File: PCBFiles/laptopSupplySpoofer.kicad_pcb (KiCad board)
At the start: 2 copper layers, 26 x 16.5 mm, 4 parts, among them J1 Screw_Terminal_01x02, J2 Screw_Terminal_01x03, U1 DS2431

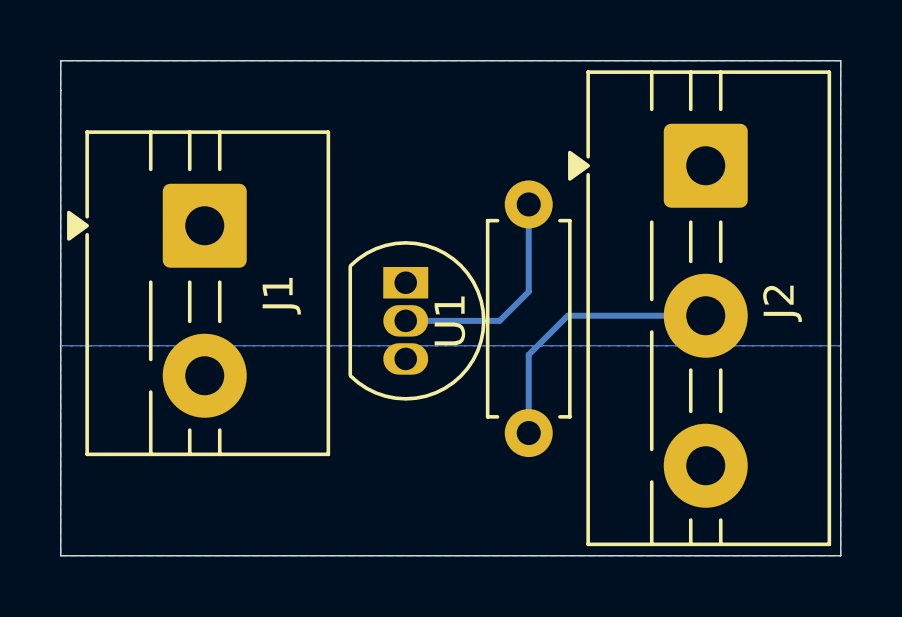
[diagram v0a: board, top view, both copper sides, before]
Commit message: removed delay_us source files and integrated it into ds2431.c for a more clean build also updated PCB files
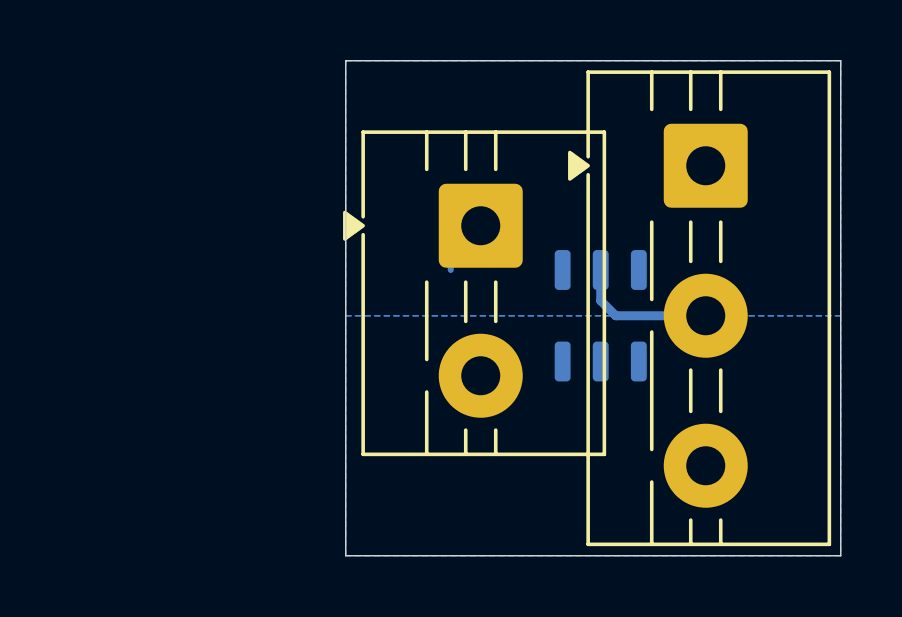
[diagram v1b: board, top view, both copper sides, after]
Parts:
- removed R1: 130, Resistor_THT:R_Axial_DIN0207_L6.3mm_D2.5mm_P7.62mm_Horizontal
- U1: value DS2431 -> DS2431P; footprint Package_TO_SOT_THT:TO-92_Inline -> Package_SO_J-Lead:TSOC-6_3.76x3.94mm_P1.27mm; moved to B.Cu
- moved J1 9.20 mm to (176.5, 89.5)
- moved U1 6.59 mm to (180.5, 92.5)
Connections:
- U1 pad 2: Net-(U1-IO) -> Net-(J2-Pin_2)
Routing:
- net Net-(U1-IO): track 7.41 -> 0.00 mm
- net Net-(J2-Pin_2): track 9.46 -> 5.14 mm
- net GND: track 0.00 -> 1.33 mm
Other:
- board size 26 x 16.5 mm -> 16.5 x 16.5 mm
